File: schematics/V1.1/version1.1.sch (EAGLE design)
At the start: 101 parts, among them IC1 ADG1604S, IC2 LM317MBSTT3, IC3 AD8610R, IC4 AD8610R, IC5 337IMP, IC6 AD8620R, Q1 16MHz, T1 BC847, T2 BC847, T3 BC847, T4 BC847, X2 BU-SMA-H

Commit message: finalize the v1.1 layout
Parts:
- added C11, C12: 100n, rcl:C-EUC0603
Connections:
- net +12V: now also C11.2
- net -12V: now also C12.1
- net AGND: now also C11.1, C12.2
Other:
- moved on the sheet: IC6P
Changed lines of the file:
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@@
 <part name="AGND17" library="supply1" deviceset="AGND" device=""/>
 <part name="GND13" library="supply1" deviceset="GND" device=""/>
+<part name="C11" library="rcl" deviceset="C-EU" device="C0603" value="100n"/>
+<part name="C12" library="rcl" deviceset="C-EU" device="C0603" value="100n"/>
 </parts>
 <sheets>
@@
 <instance part="IC6" gate="A" x="180.34" y="33.02" rot="MR180"/>
 <instance part="IC6" gate="B" x="180.34" y="12.7" rot="MR180"/>
-<instance part="IC6" gate="P" x="5.08" y="132.08"/>
+<instance part="IC6" gate="P" x="10.16" y="132.08"/>
 <instance part="R27" gate="G$1" x="180.34" y="43.18" rot="R180"/>
 <instance part="R28" gate="G$1" x="165.1" y="35.56" rot="R180"/>
@@
 <instance part="AGND17" gate="VR1" x="40.64" y="149.86" rot="R90"/>
 <instance part="GND13" gate="1" x="20.32" y="149.86" rot="R270"/>
+<instance part="C11" gate="G$1" x="5.08" y="137.16" smashed="yes" rot="R180">
+<attribute name="NAME" x="3.556" y="136.779" size="1.778" layer="95" rot="R180"/>
+<attribute name="VALUE" x="3.556" y="141.859" size="1.778" layer="96" rot="R180"/>
+</instance>
+<instance part="C12" gate="G$1" x="5.08" y="124.46" smashed="yes" rot="R180">
+<attribute name="NAME" x="3.556" y="124.079" size="1.778" layer="95" rot="R180"/>
+<attribute name="VALUE" x="3.556" y="129.159" size="1.778" layer="96" rot="R180"/>
+</instance>
 </instances>
 <busses>
@@
 <wire x1="0" y1="129.54" x2="0" y2="132.08" width="0.1524" layer="91"/>
 <junction x="0" y="132.08"/>
+<pinref part="C12" gate="G$1" pin="2"/>
+<pinref part="C11" gate="G$1" pin="1"/>
+<wire x1="5.08" y1="129.54" x2="5.08" y2="132.08" width="0.1524" layer="91"/>
+<wire x1="5.08" y1="132.08" x2="5.08" y2="134.62" width="0.1524" layer="91"/>
+<wire x1="0" y1="132.08" x2="5.08" y2="132.08" width="0.1524" layer="91"/>
+<junction x="5.08" y="132.08"/>
 </segment>
 <segment>
@@
 <junction x="-5.08" y="142.24"/>
 <pinref part="IC6" gate="P" pin="V+"/>
-<wire x1="5.08" y1="139.7" x2="5.08" y2="142.24" width="0.1524" layer="91"/>
+<wire x1="10.16" y1="139.7" x2="10.16" y2="142.24" width="0.1524" layer="91"/>
+<wire x1="10.16" y1="142.24" x2="5.08" y2="142.24" width="0.1524" layer="91"/>
+<junction x="0" y="142.24"/>
+<pinref part="C11" gate="G$1" pin="2"/>
 <wire x1="5.08" y1="142.24" x2="0" y2="142.24" width="0.1524" layer="91"/>
-<junction x="0" y="142.24"/>
+<junction x="5.08" y="142.24"/>
 </segment>
 </net>
@@
 <junction x="-5.08" y="121.92"/>
 <pinref part="IC6" gate="P" pin="V-"/>
-<wire x1="5.08" y1="124.46" x2="5.08" y2="121.92" width="0.1524" layer="91"/>
+<wire x1="10.16" y1="124.46" x2="10.16" y2="121.92" width="0.1524" layer="91"/>
+<wire x1="10.16" y1="121.92" x2="5.08" y2="121.92" width="0.1524" layer="91"/>
+<junction x="0" y="121.92"/>
+<pinref part="C12" gate="G$1" pin="1"/>
 <wire x1="5.08" y1="121.92" x2="0" y2="121.92" width="0.1524" layer="91"/>
-<junction x="0" y="121.92"/>
-</segment>
-</net>
+<junction x="5.08" y="121.92"/>
+</segment>
+</net>

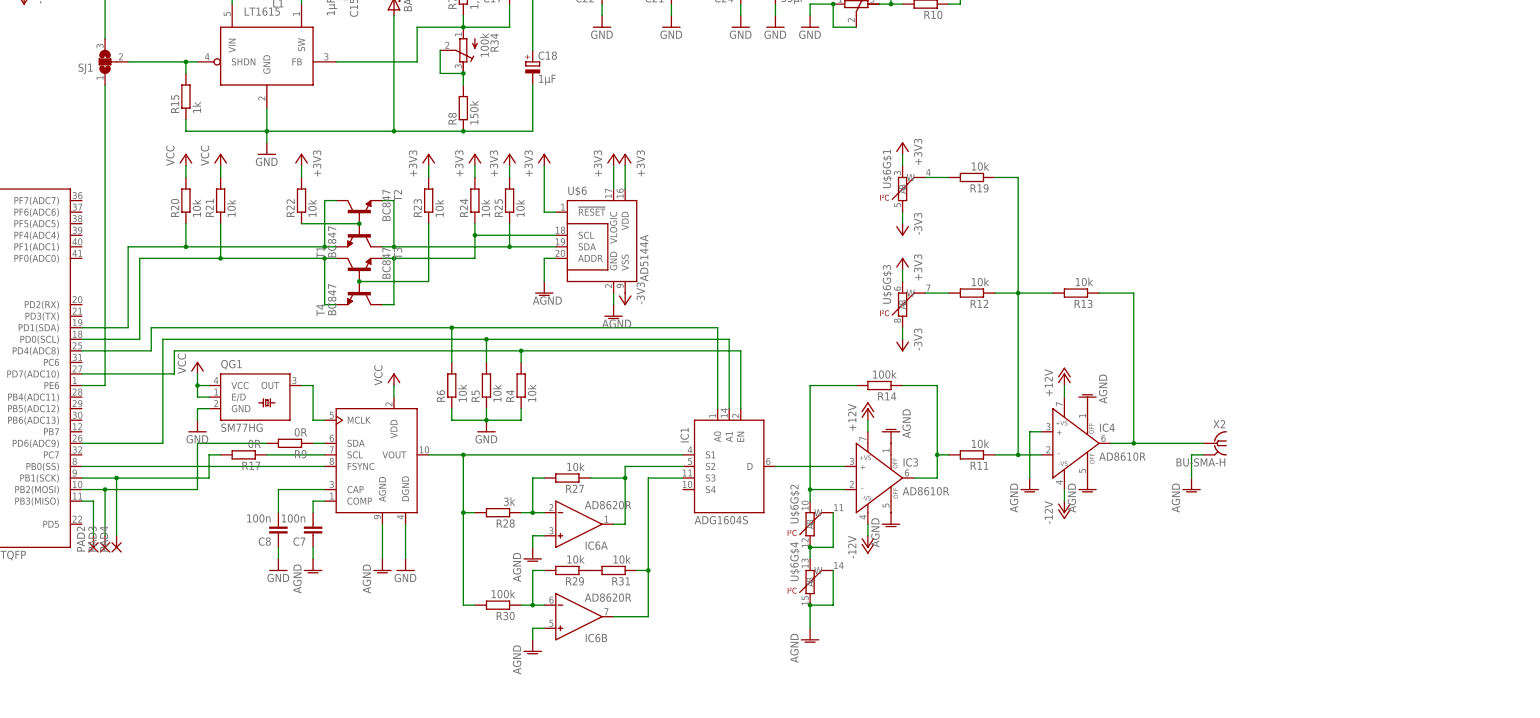
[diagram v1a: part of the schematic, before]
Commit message: restructure the circuit and pcb-layout to fix the offset issue
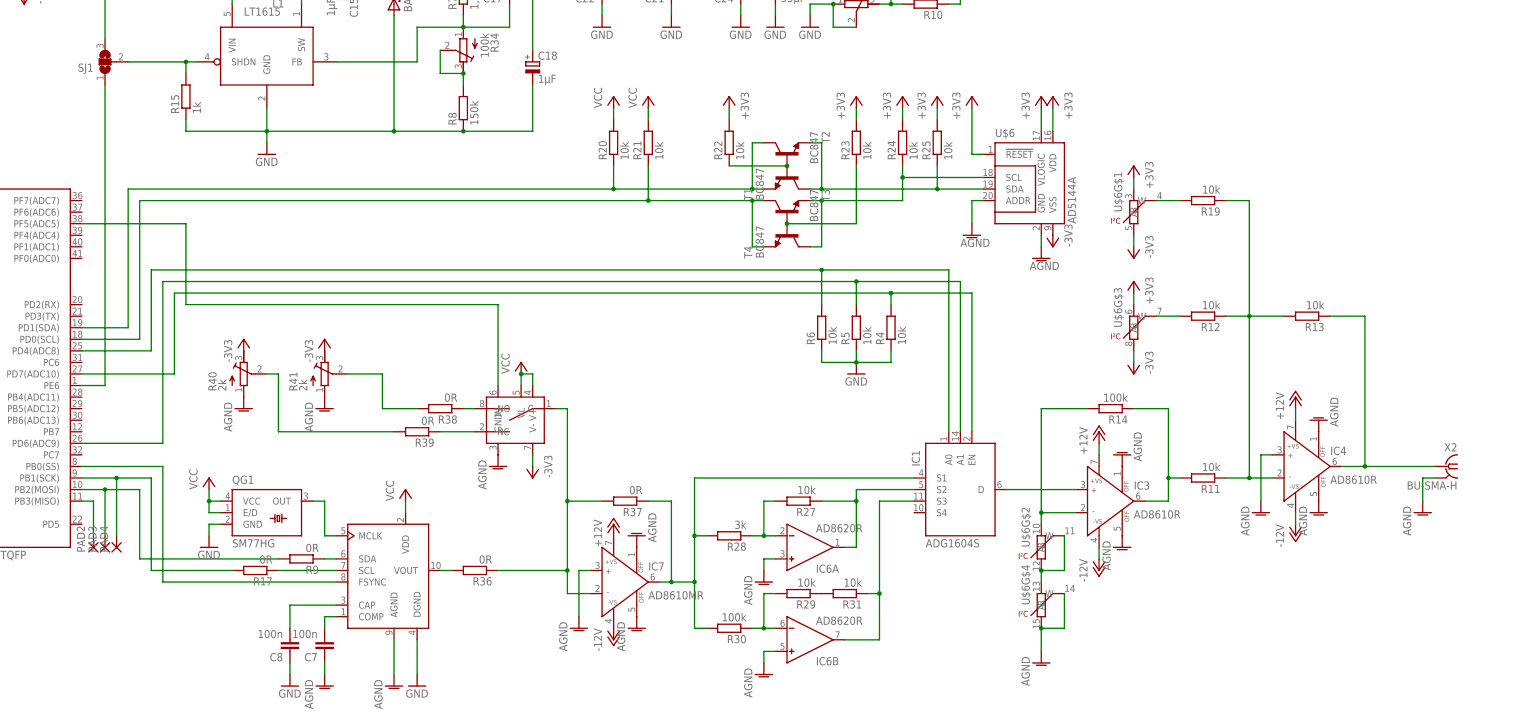
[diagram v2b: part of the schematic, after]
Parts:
- added IC7: AD8610MR, analog-devices:AD8610MR
- added R36, R37, R38, R39: 0R, rcl:R-EU_R0603
- added R40, R41: 2k, rcl:R-TRIMM3224W
- added U$12: DG419LDQ, switch:DG419LDQ
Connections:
- new net N$58: R36.2, U$1.VOUT
- new net N$59: IC7.IN-, R36.1, R37.2, U$12.C
- new net N$60: R38.1, U$12.NO
- new net N$61: U$12.IN, U$3.PF5(ADC5)
- new net N$62: R39.1, U$12.NC
- new net N$63: R39.2, R40.S
- new net N$64: R38.2, R41.S
- net +12V: now also IC7.+VS
- net -12V: now also IC7.-VS
- net -3V3: now also R40.E, R41.E, U$12.V-
- net AGND: now also IC7.IN+, IC7.OFF@1, IC7.OFF@2, R40.A, R41.A, U$12.GND
- net N$16: now also IC7.OUT, R37.1; no longer U$1.VOUT
- net VCC: now also U$12.V+, U$12.VL
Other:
- moved on the sheet: C7, C8, IC1, IC3, IC4, IC6A, IC6B, QG1, R11, R12, R13, R14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
